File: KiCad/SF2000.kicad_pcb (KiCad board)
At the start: 4 copper layers, 111.5 x 83.9 mm, 105 parts, among them J1 Conn_2Rows-86Pins_even_odd, J10 Conn_02x01, J11 Conn_02x01, J2 Conn_01x02, J20 Conn_02x11_Odd_Even, J3 Conn_02x05_Odd_Even, J4 Conn_02x01, J5 Conn_01x01, J6 Micro_SD_Card_Socket, J7 Conn_02x01, J8 Conn_02x01, J9 Conn_02x01, Q1 MMBT3904, Q2 MMBT3906, U1 LM1117-3.3, U10 IS61WV20488FBLL-10TLI, U11 IS61WV20488FBLL-10TLI, U12 IS61WV20488FBLL-10TLI, U13 IS61WV20488FBLL-10TLI, U14 SST39LF040, U15 SST39LF802C, U16 74AHCT3G14, U2 ABLIC S-1132B43-M5T1U, U20 AT25SF081B-SSH, U3 TLV74312PDBV, U4 SN74CBT16211, U5 SN74CBT16211, U6 SN74CBT16211, U7 SN74AUP1T87DCKR, U8 T8Q144C3, U9 68000D, X1 Oscillator_7.0x5.0mm

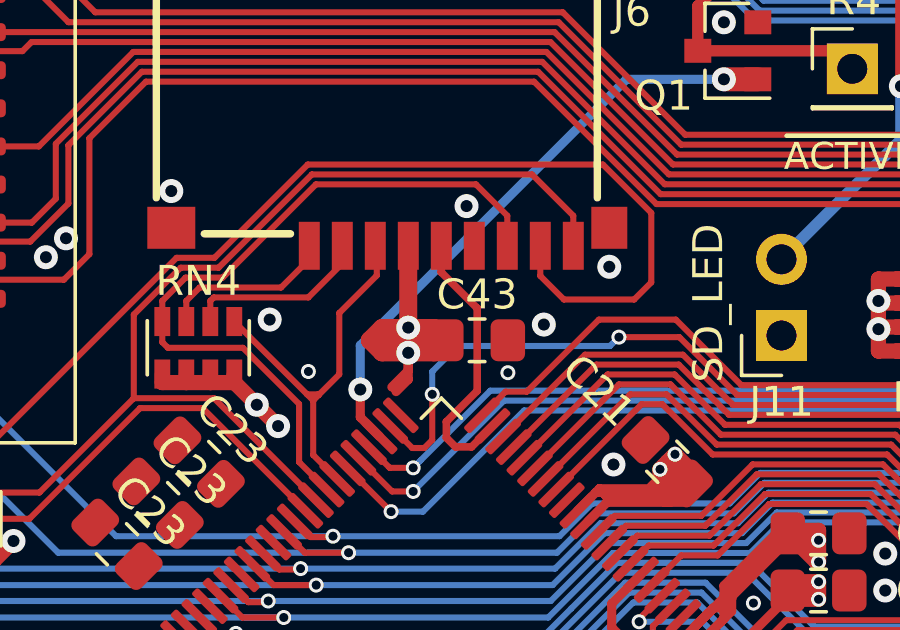
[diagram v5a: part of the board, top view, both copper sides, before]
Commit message: Routing of 3.3V supply to SD-slot Power pin via decoupling cap C43
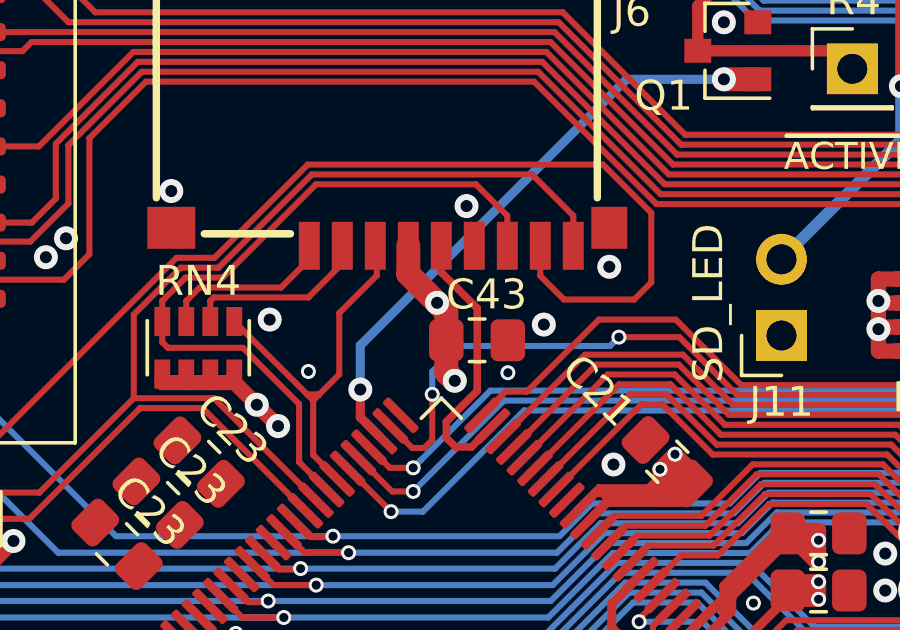
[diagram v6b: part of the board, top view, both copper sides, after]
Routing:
- net 3V3: track 311.3 -> 301.8 mm
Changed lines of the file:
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@@
     (thickness 1.6)
     (drawings 168)
-    (tracks 4466)
+    (tracks 4453)
     (zones 0)
     (modules 105)
@@
     (tags "capacitor handsolder")
     (attr smd)
-    (fp_text reference C43 (at 0 1.524) (layer F.SilkS)
+    (fp_text reference C43 (at -0.3169 1.524) (layer F.SilkS)
       (effects (font (size 1 1) (thickness 0.15)))
     )
@@
   (via (at 162.4042 86.8384) (size 0.8) (drill 0.4) (layers F.Cu B.Cu) (net 68))
   (via (at 138.4212 101.2783) (size 0.5) (drill 0.3) (layers F.Cu B.Cu) (net 68))
-  (via (at 126.9023 75.9418) (size 0.8) (drill 0.4) (layers F.Cu B.Cu) (net 68))
-  (via (at 126.9023 76.78) (size 0.8) (drill 0.4) (layers F.Cu B.Cu) (net 68))
+  (via (at 127.8642 75.1143) (size 0.8) (drill 0.4) (layers F.Cu B.Cu) (net 68))
+  (via (at 128.4542 77.7143) (size 0.8) (drill 0.4) (layers F.Cu B.Cu) (net 68))
   (segment (start 172.0292 75.1643) (end 170.9542 75.1643) (width 0.3048) (layer F.Cu) (net 68))
   (segment (start 170.6042 75.5143) (end 169.5042 75.5143) (width 0.3048) (layer F.Cu) (net 68))
@@
   (segment (start 108.4619 61.8643) (end 108.4619 63.0616) (width 0.6) (layer F.Cu) (net 68))
   (segment (start 137.43307 101.663816) (end 137.943616 101.663816) (width 0.3048) (layer F.Cu) (net 68))
-  (segment (start 127.7693 76.7673) (end 128.1723 76.3643) (width 0.6) (layer F.Cu) (net 68))
-  (segment (start 126.9023 76.7673) (end 127.7693 76.7673) (width 0.6) (layer F.Cu) (net 68))
-  (segment (start 127.7625 75.9545) (end 128.1723 76.3643) (width 0.6) (layer F.Cu) (net 68))
-  (segment (start 126.9023 75.9545) (end 127.7625 75.9545) (width 0.6) (layer F.Cu) (net 68))
-  (segment (start 127.3053 76.3643) (end 126.9023 76.7673) (width 0.6) (layer F.Cu) (net 68))
-  (segment (start 128.1723 76.3643) (end 127.3053 76.3643) (width 0.6) (layer F.Cu) (net 68))
-  (segment (start 126.0313 75.9545) (end 125.6249 76.3609) (width 0.6) (layer F.Cu) (net 68))
-  (segment (start 126.9023 75.9545) (end 126.0313 75.9545) (width 0.6) (layer F.Cu) (net 68))
-  (segment (start 126.0313 76.7673) (end 125.6249 76.3609) (width 0.6) (layer F.Cu) (net 68))
-  (segment (start 126.9023 76.7673) (end 126.0313 76.7673) (width 0.6) (layer F.Cu) (net 68))
-  (segment (start 126.4959 76.3609) (end 126.9023 75.9545) (width 0.6) (layer F.Cu) (net 68))
-  (segment (start 125.6249 76.3609) (end 126.4959 76.3609) (width 0.6) (layer F.Cu) (net 68))
-  (segment (start 126.9023 76.7673) (end 126.9023 77.3769) (width 0.3048) (layer F.Cu) (net 68))
-  (segment (start 126.9023 76.7673) (end 126.9023 77.669) (width 0.3048) (layer F.Cu) (net 68))
-  (segment (start 126.9023 76.7673) (end 126.9023 76.8816) (width 0.3048) (layer F.Cu) (net 68))
   (segment (start 126.9023 73.2162) (end 126.9042 73.2143) (width 0.6) (layer F.Cu) (net 68))
-  (segment (start 126.9023 75.9545) (end 126.9023 73.2162) (width 0.6) (layer F.Cu) (net 68))
-  (segment (start 126.9023 76.7673) (end 127.0801 76.9451) (width 0.3048) (layer F.Cu) (net 68))
-  (segment (start 126.9023 77.3769) (end 126.3562 77.923) (width 0.3048) (layer F.Cu) (net 68))
-  (segment (start 126.9023 77.669) (end 126.4959 78.0754) (width 0.3048) (layer F.Cu) (net 68))
   (segment (start 110.2018 107.4759) (end 111.0146 108.2887) (width 0.6) (layer F.Cu) (net 68))
   (via (at 142.5749 75.0528) (size 0.8) (drill 0.4) (layers F.Cu B.Cu) (net 68))
@@
   (segment (start 115.790684 99.702616) (end 115.372516 99.702616) (width 0.508) (layer F.Cu) (net 68))
   (segment (start 121.9642 104.2943) (end 121.173768 105.084732) (width 0.8) (layer F.Cu) (net 68))
+  (segment (start 128.1723 77.4324) (end 128.4542 77.7143) (width 0.8) (layer F.Cu) (net 68))
+  (segment (start 128.1723 76.3643) (end 128.1723 77.4324) (width 0.8) (layer F.Cu) (net 68))
+  (segment (start 128.1723 75.4224) (end 127.8642 75.1143) (width 0.8) (layer F.Cu) (net 68))
+  (segment (start 128.1723 76.3643) (end 128.1723 75.4224) (width 0.8) (layer F.Cu) (net 68))
+  (segment (start 126.9042 73.2143) (end 126.9042 74.1543) (width 0.8) (layer F.Cu) (net 68))
+  (segment (start 126.9042 74.1543) (end 127.8642 75.1143) (width 0.8) (layer F.Cu) (net 68))
   (segment (start 112.7672 128.6849) (end 112.7672 138.8703) (width 0.2032) (layer B.Cu) (net 69))
   (segment (start 116.2978 125.1543) (end 112.7672 128.6849) (width 0.2032) (layer B.Cu) (net 69))

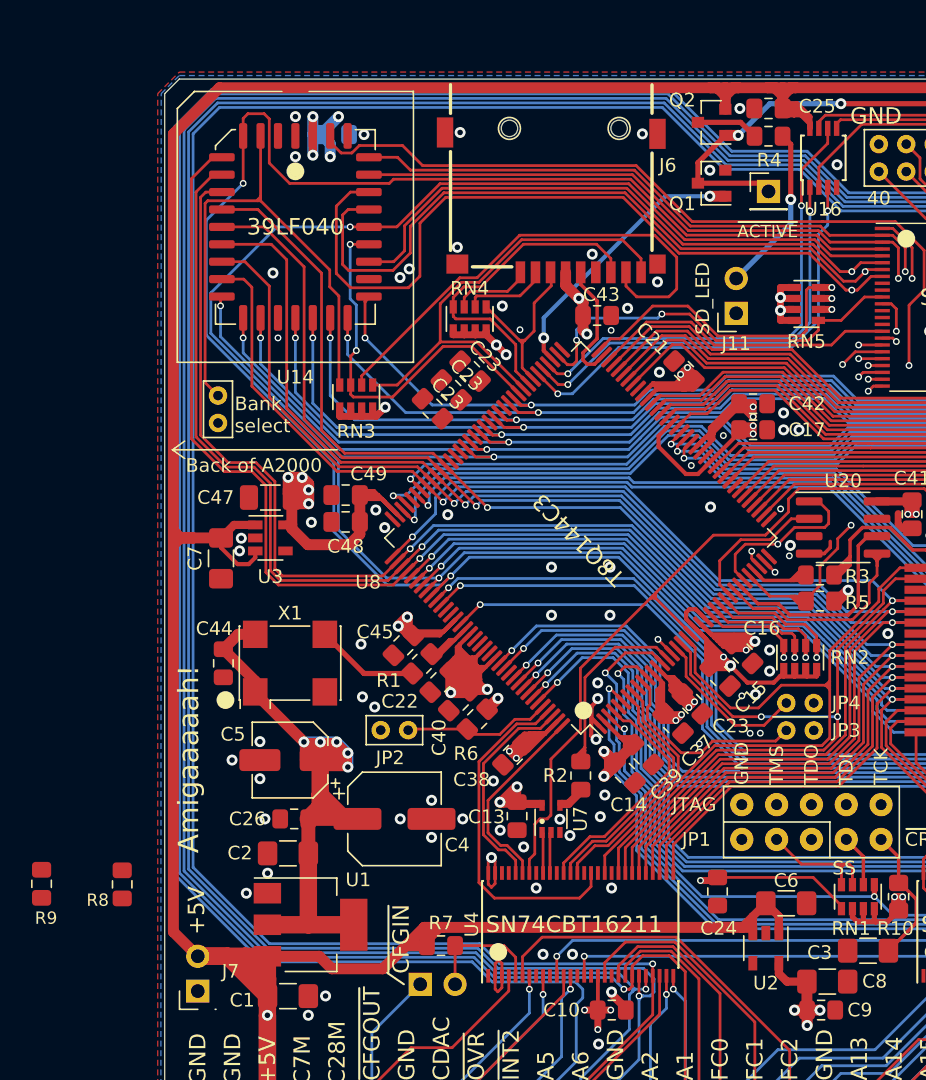
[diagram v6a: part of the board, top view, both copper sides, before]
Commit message: Change LED-circuit to active low and controlled by SD-cards CS-signal
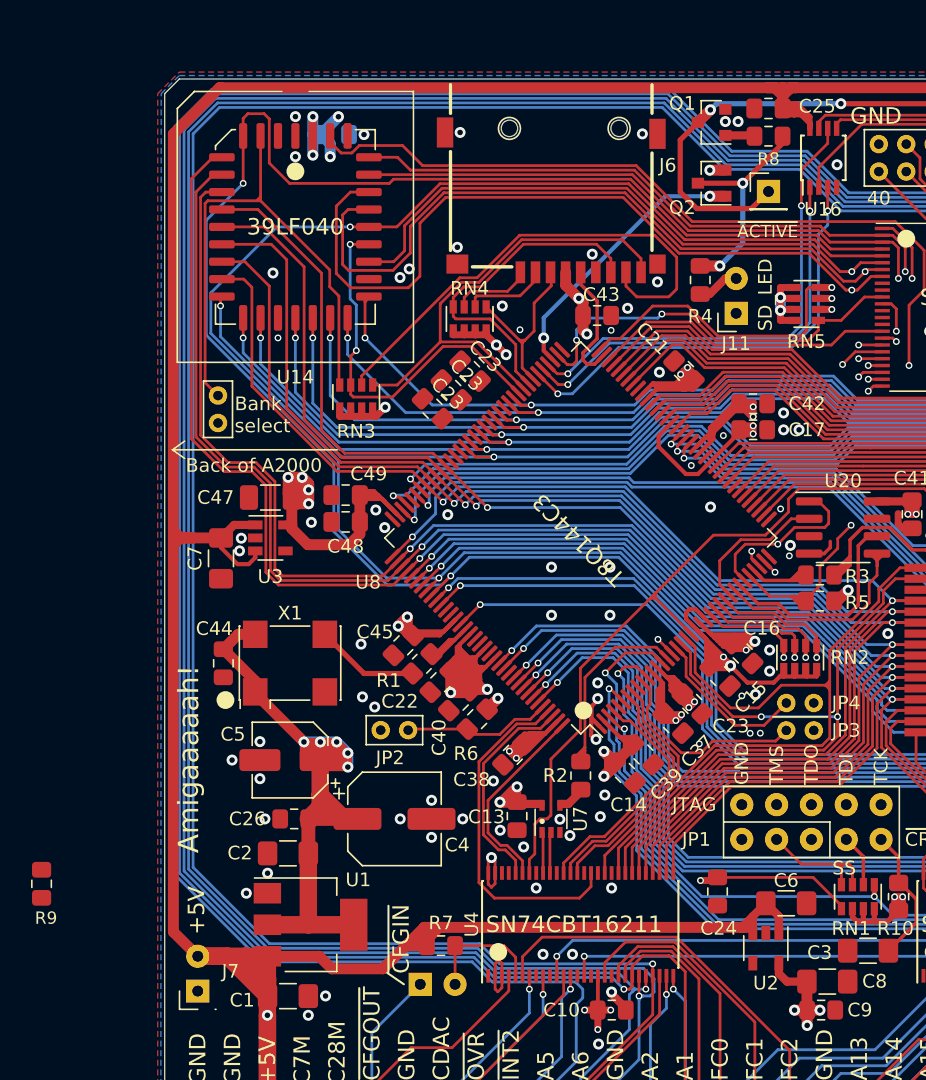
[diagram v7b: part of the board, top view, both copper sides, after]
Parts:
- R8: value 10k -> 4.7k
- moved R8 72.1 mm to (141.7, 63.3), turned to 180 degrees
- moved R4 11.6 mm to (136.7, 73.8), turned to 90 degrees
- moved Q1 4.44 mm to (137.6, 62.3)
- moved Q2 4.44 mm to (137.6, 66.7)
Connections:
- Q1 pad 1: LED_ACTIVE_3V3 -> Net-(Q1-Pad1)
- Q2 pad 1: LED_ACTIVE_n -> SD_CS
- Q2 pad 2: +5VDC -> 3V3
- R8 pad 1: 3V3 -> Net-(Q2-Pad3)
- R8 pad 2: Net-(R8-Pad2) -> Net-(Q1-Pad1)
- R9 pad 2: Net-(R8-Pad2) -> Net-(R9-Pad2)
- U8 pad 75: LED_ACTIVE_3V3 -> SD_CS
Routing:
- net SD_CS: track 0.00 -> 20.2 mm, vias 0 -> 2
- net LED_ACTIVE_3V3: track 20.2 -> 0.00 mm, vias 2 -> 0
- net Net-(Q2-Pad3): track 4.93 -> 16.1 mm, vias 0 -> 2
- net /SF2000_FPGA/SD_LED: track 12.3 -> 3.09 mm, vias 1 -> 0
- net LED_ACTIVE_n: track 45.8 -> 51.6 mm
- net +5VDC: track 271.6 -> 267.4 mm
- net Net-(Q1-Pad1): track 0.00 -> 2.15 mm
- net 3V3: track 301.8 -> 303.9 mm, vias 50 -> 51
